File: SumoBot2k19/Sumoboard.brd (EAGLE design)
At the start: 80 x 60 mm, 38 parts

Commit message: connected sensors :DD
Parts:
- moved BR_REF 7.49 mm to (2.79, 53.3), turned to 270 degrees
- moved FL_REF 6.33 mm to (77.2, 6.71), turned to 90 degrees
- moved BL_REF 4.84 mm to (27.5, 2.13), turned to 180 degrees
- moved C6 0.22 mm to (4.98, 27.2)
- moved C7 0.22 mm to (6.50, 27.2)
- moved C9 0.22 mm to (62.6, 20.4)
- moved C8 0.15 mm to (5.17, 23.2)
- moved FR_REF 0.06 mm to (77.2, 53.3)
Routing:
- net BL_REF: track 0.00 -> 36.5 mm
- net BR_REF: track 0.00 -> 33.9 mm
- net VOUT_IR: track 0.00 -> 33.7 mm
- net FL_REF: track 12.6 -> 43.2 mm
- net FR_REF: track 0.00 -> 26.2 mm
- net RIGHT_DIR: track 0.00 -> 24.3 mm
- net RIGHT_PWM: track 0.00 -> 24.0 mm
- net XSHUT_FL: track 0.00 -> 17.8 mm
- net GND: track 28.0 -> 16.3 mm
- net 3.3V: track 16.9 -> 6.19 mm
- net XSHUT_F: track 0.00 -> 6.87 mm
- net VREG: track 0.00 -> 3.97 mm
- net VIN: track 29.6 -> 26.5 mm

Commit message: need to check battery connection
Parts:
- moved C12 4.53 mm to (12.0, 19.9)
- moved C8 0.15 mm to (5.02, 23.2)
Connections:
- removed net GPIO: FL_TOF.1, FR_TOF.1, F_TOF.1, L_TOF.1, R_TOF.1
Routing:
- net XSHUT_R: track 0.00 -> 28.5 mm
- net SCL: track 146.0 -> 160.3 mm
- net SDA: track 145.4 -> 156.9 mm
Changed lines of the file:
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@@
 <attribute name="VALUE" x="26.416" y="21.161996875" size="0.6096" layer="27" font="vector" ratio="20" rot="R180" align="top-center"/>
 </element>
-<element name="C12" library="SparkFun-Capacitors" library_urn="urn:adsk.eagle:library:510" package="0603" package3d_urn="urn:adsk.eagle:package:37414/1" value="0.1uF" x="13.49499375" y="24.209996875" smashed="yes" rot="R180">
-<attribute name="NAME" x="13.49499375" y="25.479996875" size="0.6096" layer="25" font="vector" ratio="20" rot="R180" align="bottom-center"/>
-<attribute name="PROD_ID" value="CAP-08604" x="-5.55500625" y="115.649996875" size="1.778" layer="27" rot="R180" display="off"/>
-<attribute name="VALUE" x="13.49499375" y="24.971996875" size="0.6096" layer="27" font="vector" ratio="20" rot="R180" align="top-center"/>
+<element name="C12" library="SparkFun-Capacitors" library_urn="urn:adsk.eagle:library:510" package="0603" package3d_urn="urn:adsk.eagle:package:37414/1" value="0.1uF" x="11.97099375" y="19.942796875" smashed="yes" rot="R180">
+<attribute name="NAME" x="11.97099375" y="21.212796875" size="0.6096" layer="25" font="vector" ratio="20" rot="R180" align="bottom-center"/>
+<attribute name="PROD_ID" value="CAP-08604" x="-7.07900625" y="111.382796875" size="1.778" layer="27" rot="R180" display="off"/>
+<attribute name="VALUE" x="11.97099375" y="20.704796875" size="0.6096" layer="27" font="vector" ratio="20" rot="R180" align="top-center"/>
 </element>
 <element name="C2" library="SparkFun-Capacitors" library_urn="urn:adsk.eagle:library:510" package="0603" package3d_urn="urn:adsk.eagle:package:37414/1" value="0.1uF" x="14.478" y="55.84700625" smashed="yes" rot="R205">
@@
 <attribute name="VALUE" x="5.7404" y="27.23639375" size="0.6096" layer="27" font="vector" ratio="20" rot="R270" align="top-center"/>
 </element>
-<element name="C8" library="SparkFun-Capacitors" library_urn="urn:adsk.eagle:library:510" package="0603" package3d_urn="urn:adsk.eagle:package:37414/1" value="1.0uF" x="5.17400625" y="23.2156" smashed="yes" rot="R270">
-<attribute name="NAME" x="4.92000625" y="21.1836" size="0.6096" layer="25" font="vector" ratio="20" align="bottom-center"/>
-<attribute name="PROD_ID" value="CAP-00868" x="-81.18599375" y="-36.4744" size="1.778" layer="27" rot="R270" display="off"/>
-<attribute name="VALUE" x="4.41200625" y="23.2156" size="0.6096" layer="27" font="vector" ratio="20" rot="R270" align="top-center"/>
+<element name="C8" library="SparkFun-Capacitors" library_urn="urn:adsk.eagle:library:510" package="0603" package3d_urn="urn:adsk.eagle:package:37414/1" value="1.0uF" x="5.02160625" y="23.2156" smashed="yes" rot="R270">
+<attribute name="NAME" x="4.76760625" y="21.1836" size="0.6096" layer="25" font="vector" ratio="20" align="bottom-center"/>
+<attribute name="PROD_ID" value="CAP-00868" x="-81.33839375" y="-36.4744" size="1.778" layer="27" rot="R270" display="off"/>
+<attribute name="VALUE" x="4.25960625" y="23.2156" size="0.6096" layer="27" font="vector" ratio="20" rot="R270" align="top-center"/>
 </element>
 <element name="C9" library="SparkFun-Capacitors" library_urn="urn:adsk.eagle:library:510" package="0603" package3d_urn="urn:adsk.eagle:package:37414/1" value="0.1uF" x="62.59319375" y="20.399996875" smashed="yes" rot="R180">
@@
 <wire x1="29.972" y1="17.78" x2="46.5192" y2="18.143084375" width="0" layer="19" extent="1-1"/>
 <wire x1="27.266" y1="20.399996875" x2="29.972" y2="17.78" width="0" layer="19" extent="1-1"/>
-<wire x1="14.34499375" y1="24.209996875" x2="27.266" y2="20.399996875" width="0" layer="19" extent="1-1"/>
-<wire x1="12.065" y1="22.225" x2="14.34499375" y2="24.209996875" width="0" layer="19" extent="1-1"/>
-<wire x1="5.17400625" y1="22.3656" x2="3.33499375" y2="22.225" width="0" layer="19" extent="1-1"/>
+<wire x1="12.82099375" y1="19.942796875" x2="27.266" y2="20.399996875" width="0" layer="19" extent="1-1"/>
+<wire x1="13.02260625" y1="14.3256" x2="12.82099375" y2="19.942796875" width="0" layer="19" extent="1-1"/>
+<wire x1="5.02160625" y1="22.3656" x2="3.33499375" y2="22.225" width="0" layer="19" extent="1-1"/>
 </signal>
 <signal name="GND">
@@
 <wire x1="25.566" y1="20.399996875" x2="27.432" y2="30.48" width="0" layer="19" extent="1-1"/>
 <wire x1="27.432" y1="17.78" x2="25.566" y2="20.399996875" width="0" layer="19" extent="1-1"/>
-<wire x1="12.64499375" y1="24.209996875" x2="25.566" y2="20.399996875" width="0" layer="19" extent="1-1"/>
-<wire x1="6.5024" y1="26.38639375" x2="12.64499375" y2="24.209996875" width="0" layer="19" extent="1-1"/>
+<wire x1="11.12099375" y1="19.942796875" x2="25.566" y2="20.399996875" width="0" layer="19" extent="1-1"/>
+<wire x1="6.5024" y1="26.38639375" x2="11.12099375" y2="19.942796875" width="0" layer="19" extent="1-1"/>
 <wire x1="4.9784" y1="26.38639375" x2="6.5024" y2="26.38639375" width="0" layer="19" extent="1-1"/>
-<wire x1="5.17400625" y1="24.0656" x2="4.9784" y2="26.38639375" width="0" layer="19" extent="1-1"/>
+<wire x1="5.02160625" y1="24.0656" x2="4.9784" y2="26.38639375" width="0" layer="19" extent="1-1"/>
 <wire x1="2.54" y1="25.55999375" x2="4.9784" y2="26.38639375" width="0" layer="19" extent="1-1"/>
 <wire x1="10.414" y1="30.48" x2="6.5024" y2="26.38639375" width="0" layer="19" extent="1-1"/>
 <wire x1="11.6864" y1="38.526725" x2="11.43" y2="38.1" width="0" layer="19" extent="1-16"/>
-<wire x1="10.414" y1="17.78" x2="12.64499375" y2="24.209996875" width="0" layer="19" extent="1-1"/>
+<wire x1="10.414" y1="17.78" x2="11.12099375" y2="19.942796875" width="0" layer="19" extent="1-1"/>
 <wire x1="3.048" y1="12.09799375" x2="10.414" y2="17.78" width="0" layer="19" extent="1-1"/>
 <wire x1="2.794" y1="53.34" x2="9.252678125" y2="39.88575625" width="0" layer="19" extent="1-1"/>
@@
 <wire x1="39.99991875" y1="55.72000625" x2="39.99991875" y2="58.902621875" width="0.1524" layer="16"/>
 <wire x1="39.99991875" y1="58.902621875" x2="40.005" y2="58.907703125" width="0.1524" layer="16"/>
-<wire x1="39.99991875" y1="55.72000625" x2="46.355" y2="49.37000625" width="0" layer="19" extent="1-1"/>
+<wire x1="46.355" y1="49.37000625" x2="44.82340625" y2="50.9016" width="0.1524" layer="16"/>
+<wire x1="39.99991875" y1="51.44008125" x2="39.99991875" y2="55.72000625" width="0.1524" layer="16"/>
+<wire x1="44.82340625" y1="50.9016" x2="40.5384" y2="50.9016" width="0.1524" layer="16"/>
+<wire x1="40.5384" y1="50.9016" x2="39.99991875" y2="51.44008125" width="0.1524" layer="16"/>
 </signal>
 <signal name="SCL">
@@
 <wire x1="16.747978125" y1="58.907703125" x2="37.45991875" y2="58.907703125" width="0.1524" layer="1"/>
 <wire x1="37.45991875" y1="58.907703125" x2="58.403978125" y2="58.907703125" width="0.1524" layer="1"/>
-<wire x1="58.42" y1="58.907703125" x2="78.9078" y2="58.907703125" width="0.1524" layer="1"/>
+<wire x1="58.403978125" y1="58.907703125" x2="78.9078" y2="58.907703125" width="0.1524" layer="1"/>
 <wire x1="78.9078" y1="58.907703125" x2="78.9078" y2="39.88575625" width="0.1524" layer="1"/>
 <wire x1="37.45991875" y1="55.72000625" x2="37.45991875" y2="58.907703125" width="0.1524" layer="1"/>
 <wire x1="16.747978125" y1="53.122553125" x2="16.747978125" y2="58.907703125" width="0.1524" layer="1"/>
 <wire x1="58.403978125" y1="55.26945625" x2="58.403978125" y2="58.907703125" width="0.1524" layer="1"/>
-<wire x1="58.403978125" y1="58.907703125" x2="58.42" y2="58.907703125" width="0.1524" layer="1"/>
-<wire x1="58.403978125" y1="55.26945625" x2="48.895" y2="49.37000625" width="0" layer="19" extent="1-1"/>
+<wire x1="58.403978125" y1="55.26945625" x2="58.403978125" y2="51.241178125" width="0.1524" layer="16"/>
+<wire x1="58.403978125" y1="51.241178125" x2="58.0644" y2="50.9016" width="0.1524" layer="16"/>
+<wire x1="50.42659375" y1="50.9016" x2="48.895" y2="49.37000625" width="0.1524" layer="16"/>
+<wire x1="58.0644" y1="50.9016" x2="50.42659375" y2="50.9016" width="0.1524" layer="16"/>
 </signal>
 <signal name="XSHUT_L">
@@
 <wire x1="4.3546375" y1="34.0485" x2="5.6371375" y2="32.766" width="0.1524" layer="1"/>
 <wire x1="5.6371375" y1="32.766" x2="24.6888" y2="32.766" width="0.1524" layer="1"/>
+<wire x1="24.6888" y1="32.766" x2="24.8412" y2="32.766" width="0.1524" layer="1"/>
 <wire x1="26.035" y1="34.13000625" x2="24.6888" y2="32.78380625" width="0.1524" layer="1"/>
 <wire x1="24.6888" y1="32.78380625" x2="24.6888" y2="32.766" width="0.1524" layer="1"/>
-</signal>
-<signal name="GPIO">
-<contactref element="L_TOF" pad="1"/>
-<contactref element="FL_TOF" pad="1"/>
-<contactref element="F_TOF" pad="1"/>
-<contactref element="FR_TOF" pad="1"/>
-<contactref element="R_TOF" pad="1"/>
-<wire x1="2.72195625" y1="32.102746875" x2="2.9098625" y2="32.290653125" width="0.3302" layer="1"/>
-<wire x1="67.48195625" y1="43.7772625" x2="53.799934375" y2="57.41635625" width="0" layer="19" extent="1-1"/>
-<wire x1="32.37991875" y1="55.72000625" x2="53.799934375" y2="57.41635625" width="0" layer="19" extent="1-1"/>
-<wire x1="12.143934375" y1="50.975653125" x2="32.37991875" y2="55.72000625" width="0" layer="19" extent="1-1"/>
-<wire x1="2.9098625" y1="32.290653125" x2="12.143934375" y2="50.975653125" width="0" layer="19" extent="1-1"/>
 </signal>
 <signal name="VREG">
@@
 <contactref element="R_TOF" pad="2"/>
 <contactref element="B1" pad="7"/>
-<wire x1="43.815" y1="34.13000625" x2="69.1146375" y2="41.831509375" width="0" layer="19" extent="1-1"/>
+<wire x1="69.1146375" y1="41.831509375" x2="62.639928125" y2="35.3568" width="0.1524" layer="1"/>
+<wire x1="45.04179375" y1="35.3568" x2="43.815" y2="34.13000625" width="0.1524" layer="1"/>
+<wire x1="62.639928125" y1="35.3568" x2="45.04179375" y2="35.3568" width="0.1524" layer="1"/>
 </signal>
 <signal name="FL_REF">

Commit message: added rats nest
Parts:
- moved C9 0.22 mm to (62.7, 20.6)
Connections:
- new net BAT: BATTERY.1, SWITCH.1
- net VBAT: no longer BATTERY.1, SWITCH.1
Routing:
- net VBAT: track 21.1 -> 0.00 mm
- net BAT: track 0.00 -> 8.62 mm
- net GND: track 16.3 -> 10.7 mm
- net 3.3V: track 6.19 -> 3.42 mm
- added copper zone on layer 1, net 3.3V
- added copper zone on layer 16, net GND

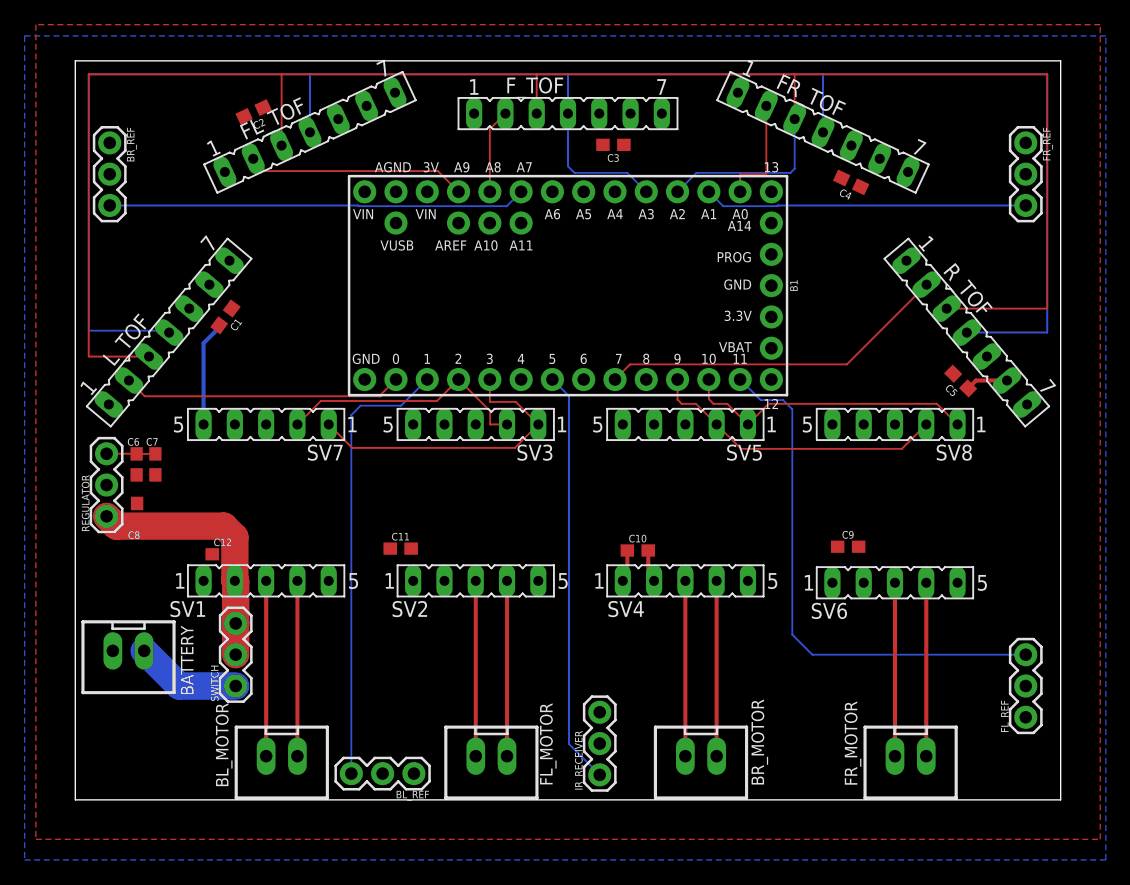
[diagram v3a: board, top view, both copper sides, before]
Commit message: routed GND and VIN
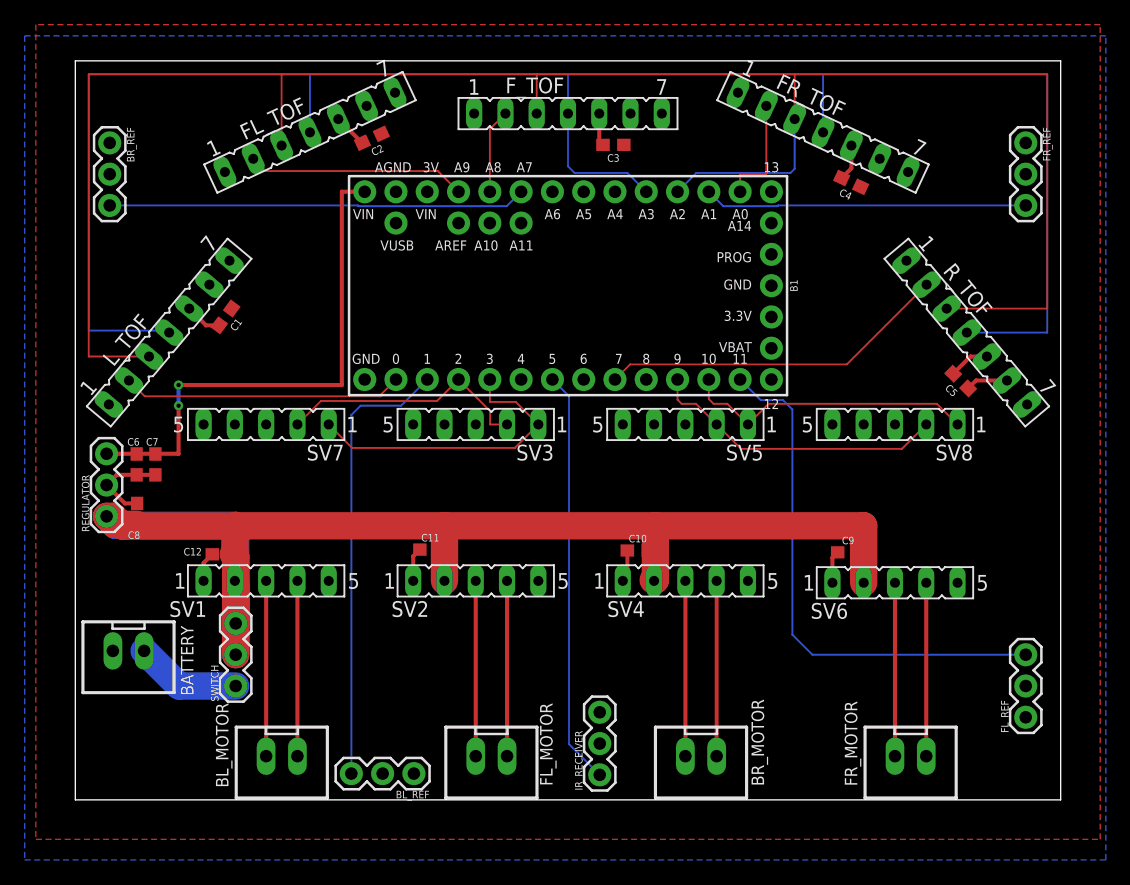
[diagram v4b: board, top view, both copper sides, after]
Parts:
- moved C2 9.84 mm to (24.1, 53.7)
- moved C11 2.41 mm to (28.8, 20.3)
- moved C9 0.46 mm to (62.7, 20.1)
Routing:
- net VIN: track 26.5 -> 122.5 mm
- net VREG: track 3.97 -> 42.4 mm, vias 0 -> 2
- net GND: track 10.7 -> 32.6 mm
- net SCL: track 160.3 -> 159.7 mm
